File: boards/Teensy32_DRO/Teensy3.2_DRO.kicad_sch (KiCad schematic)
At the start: 3 parts, among them U1 Teensy3.2, U2 Driver_Display_Ili9341TFT, U3 RS485_2_TTL_UART

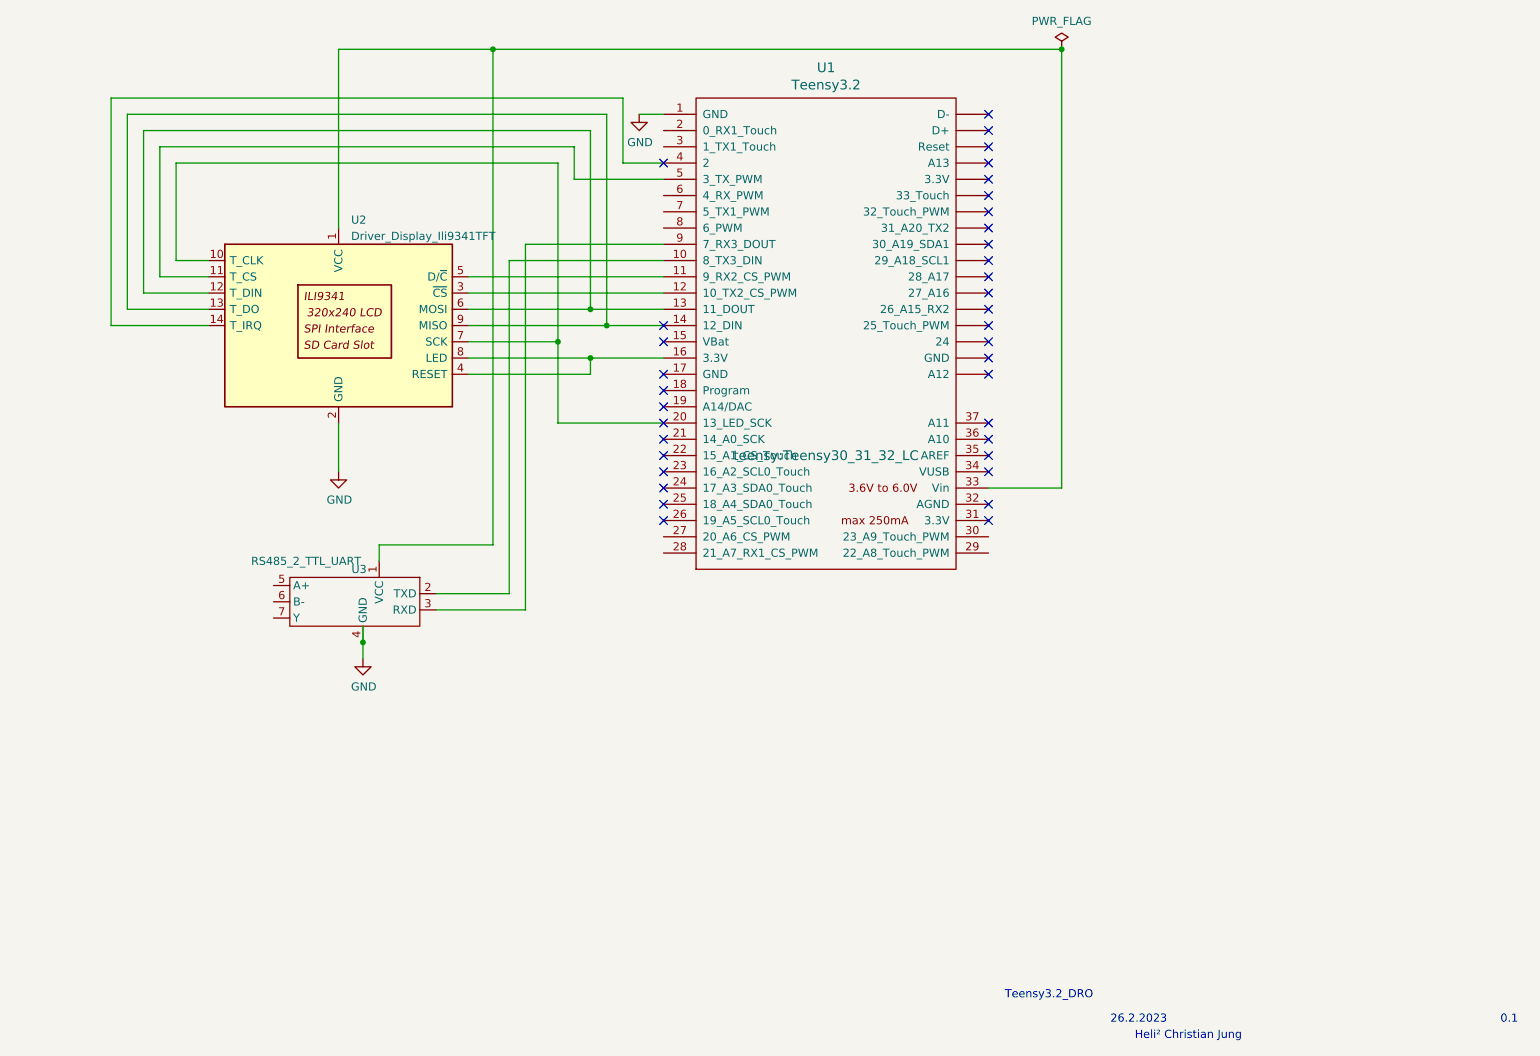
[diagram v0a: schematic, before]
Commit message: add emv circuits
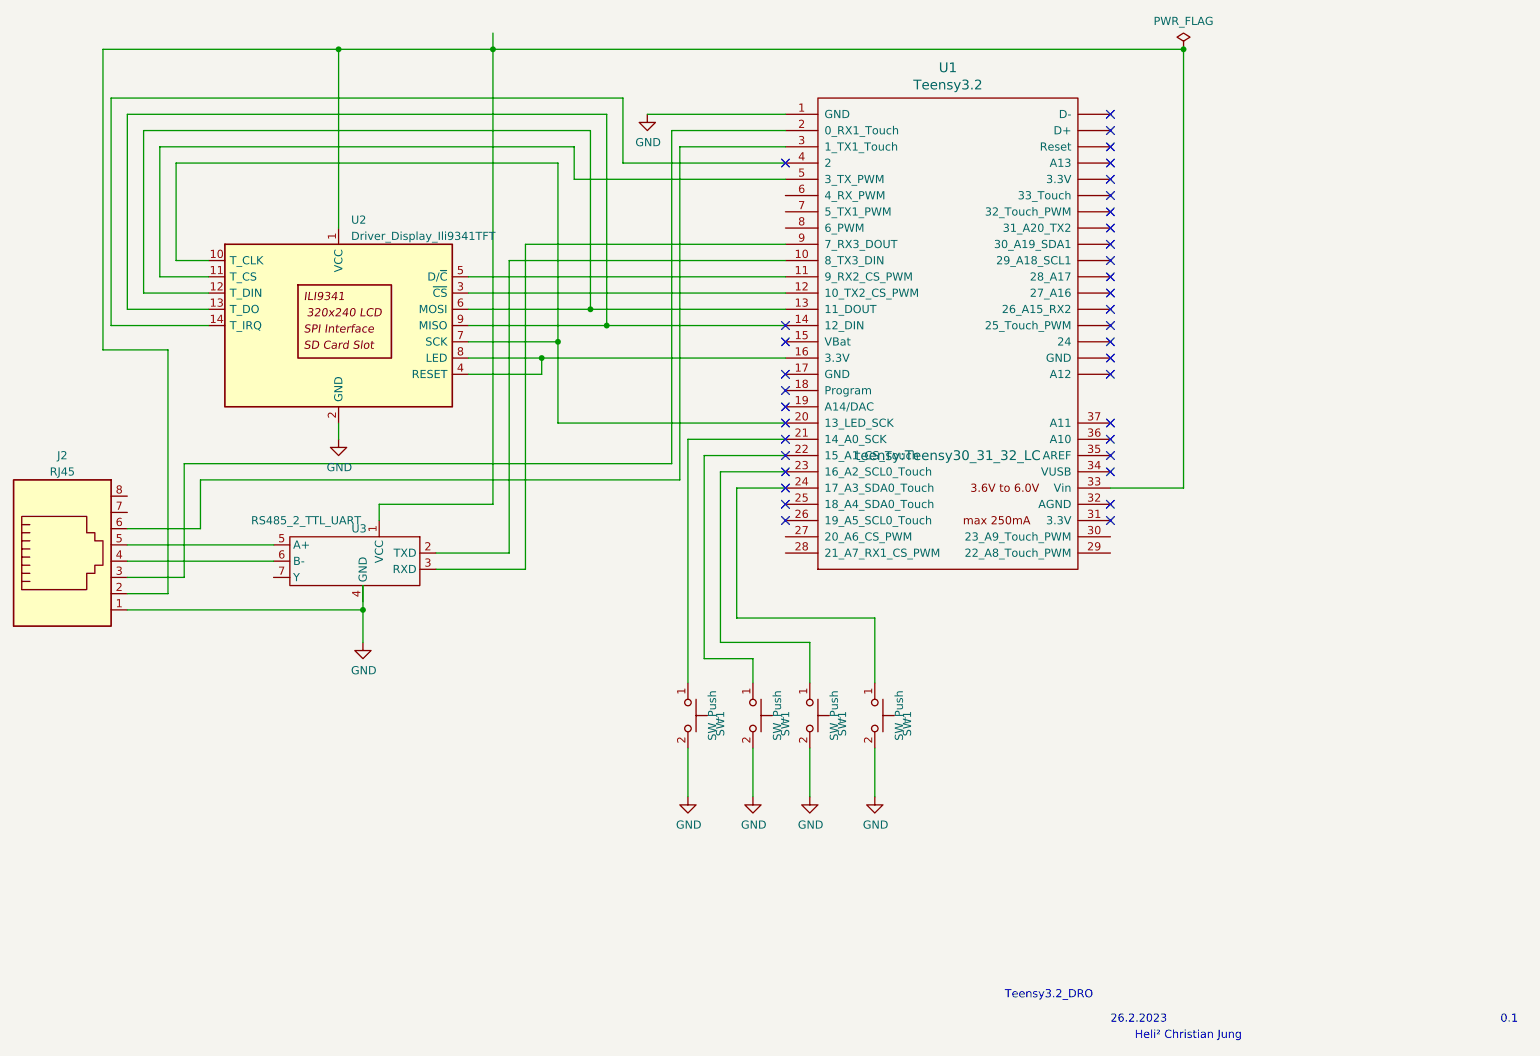
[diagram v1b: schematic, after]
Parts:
- added J2: RJ45, symbol Connector:RJ45
- added SW1 (x4): SW_Push, Heli2:Drucktaster_12x12, symbol Switch:SW_Push
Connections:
- net GND: now also J2.1, SW1.2, SW1.2, SW1.2, SW1.2; no longer U3.4 (GND)
- net at U1.2 (0_RX1_Touch): now also J2.3
- net at U1.21 (14_A0_SCK): now also SW1.1
- net at U1.22 (15_A1_CS_Touch): now also SW1.1
- net at U1.23 (16_A2_SCL0_Touch): now also SW1.1
- net at U1.24 (17_A3_SDA0_Touch): now also SW1.1
- net at U1.3 (1_TX1_Touch): now also J2.6
- net at U1.33 (Vin), U2.1 (VCC), U3.1 (VCC): now also J2.2
- net at U3.5 (A+): now also J2.5
- net at U3.6 (B-): now also J2.4
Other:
- moved on the sheet: U1, U3
